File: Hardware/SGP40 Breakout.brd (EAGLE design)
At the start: 25.4 x 25.4 mm, 44 parts, among them J2 QWIIC_RIGHT_ANGLE, J4 QWIIC_RIGHT_ANGLE, U1 SGP40

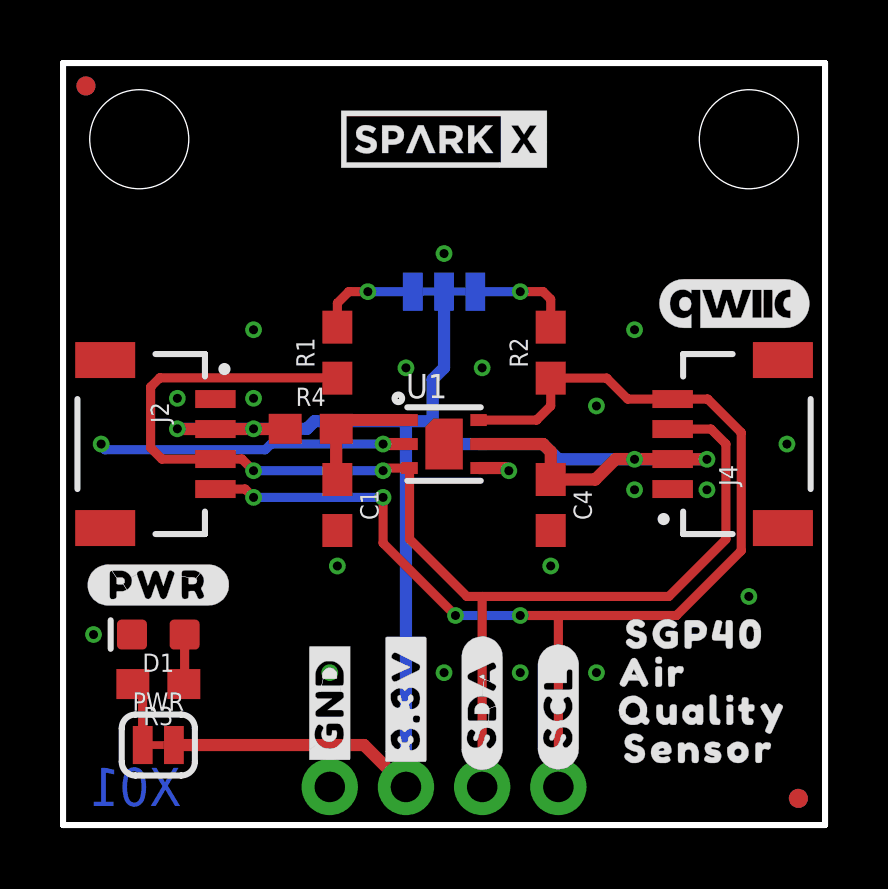
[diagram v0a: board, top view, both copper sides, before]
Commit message: Remove New-Parts. Tweak 0.3mm drill size.
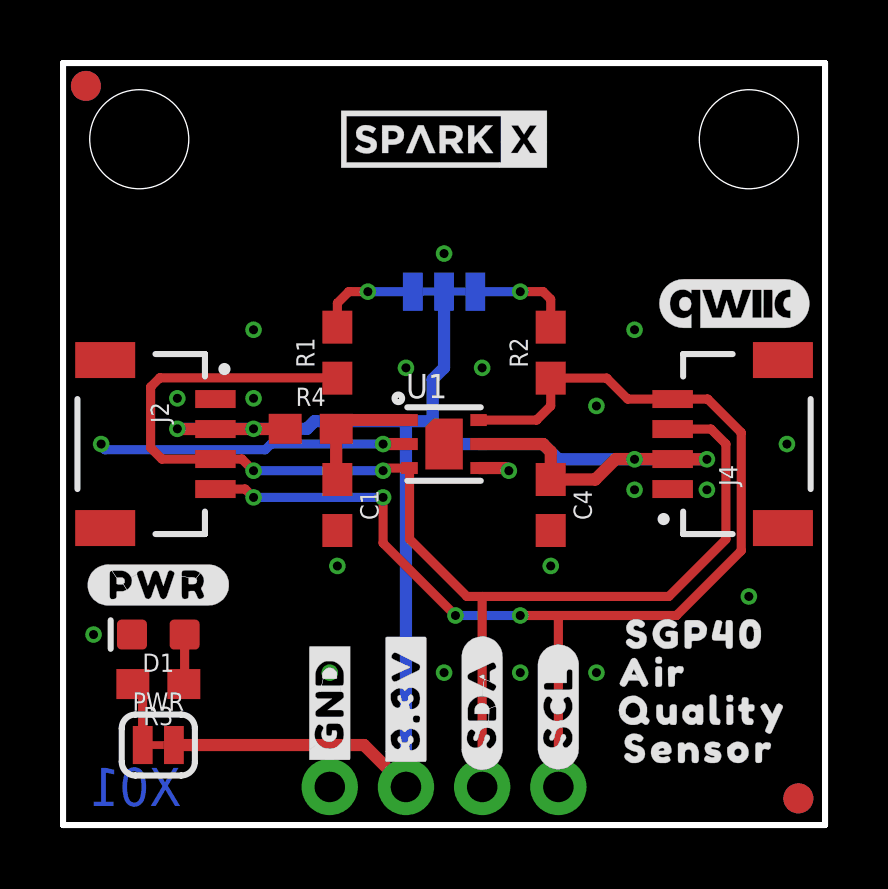
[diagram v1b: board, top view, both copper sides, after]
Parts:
- JP1, JP2, JP5, JP6: value FIDUCIALUFIDUCIAL -> FIDUCIAL1X2; device SparkFun:MICRO-FIDUCIAL -> SparkFun-Aesthetics:FIDUCIAL-1X2
- JP3, JP4: device SparkFun:STAND-OFF -> SparkFun-Hardware:STAND-OFF
- R4: device New-Parts_SparkFun-Resistors:0603 -> SparkFun-Resistors:0603
- U1: device New-Parts_SparkFun-Sensors:SGP40 -> SparkFun-Sensors:SGP40
